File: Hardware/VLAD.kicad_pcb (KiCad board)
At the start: 2 copper layers, 90 x 80 mm, 100 parts, among them J1 BMP388, J2 BNO055, J3 Micro_SD_Card, J4 Conn_01x02_Male, J5 Conn_01x03_Male, J6 Conn_01x02_Male, P1 USB_C_Plug_USB2.0, Q1 S8050, Q2 S8050, Q3 S8550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

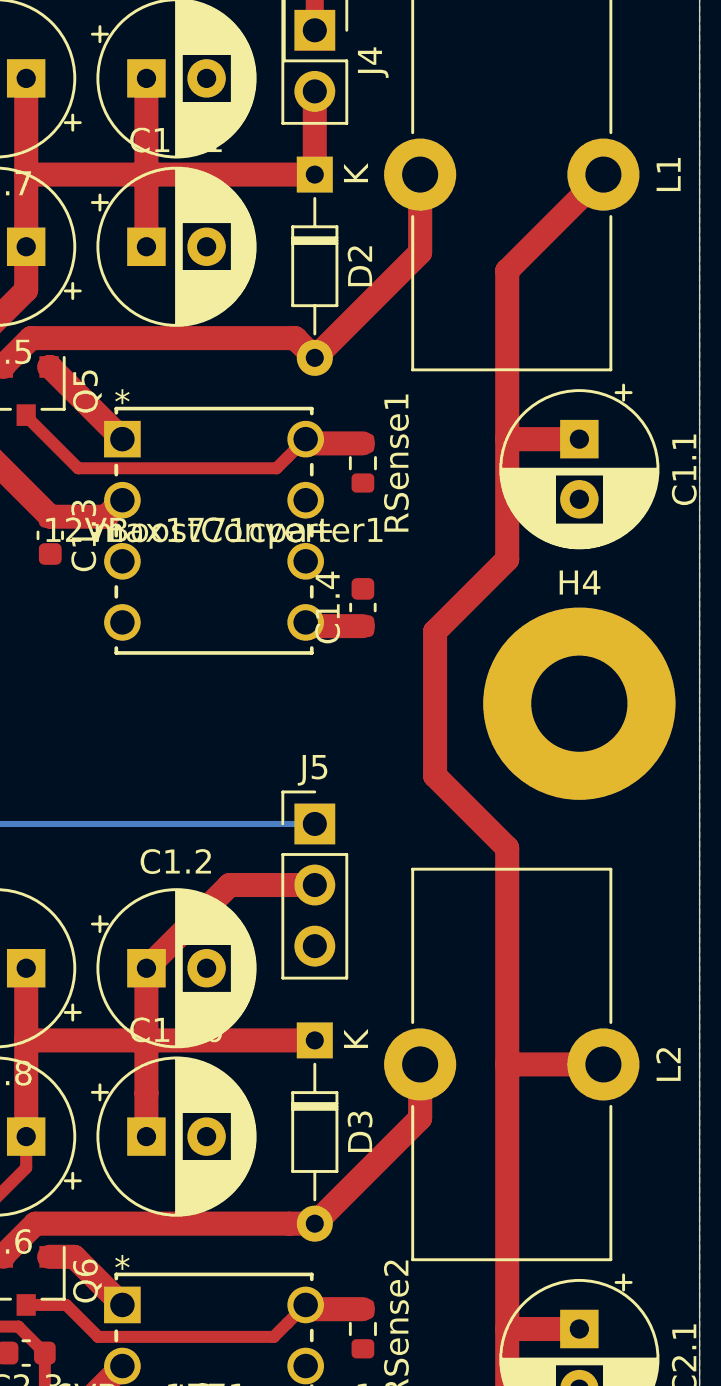
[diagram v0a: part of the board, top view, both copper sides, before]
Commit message: Need some THT - SMD changes
Inductors, capacitors, MAX1771CSA, the LED dudes and the ones next to the ESP
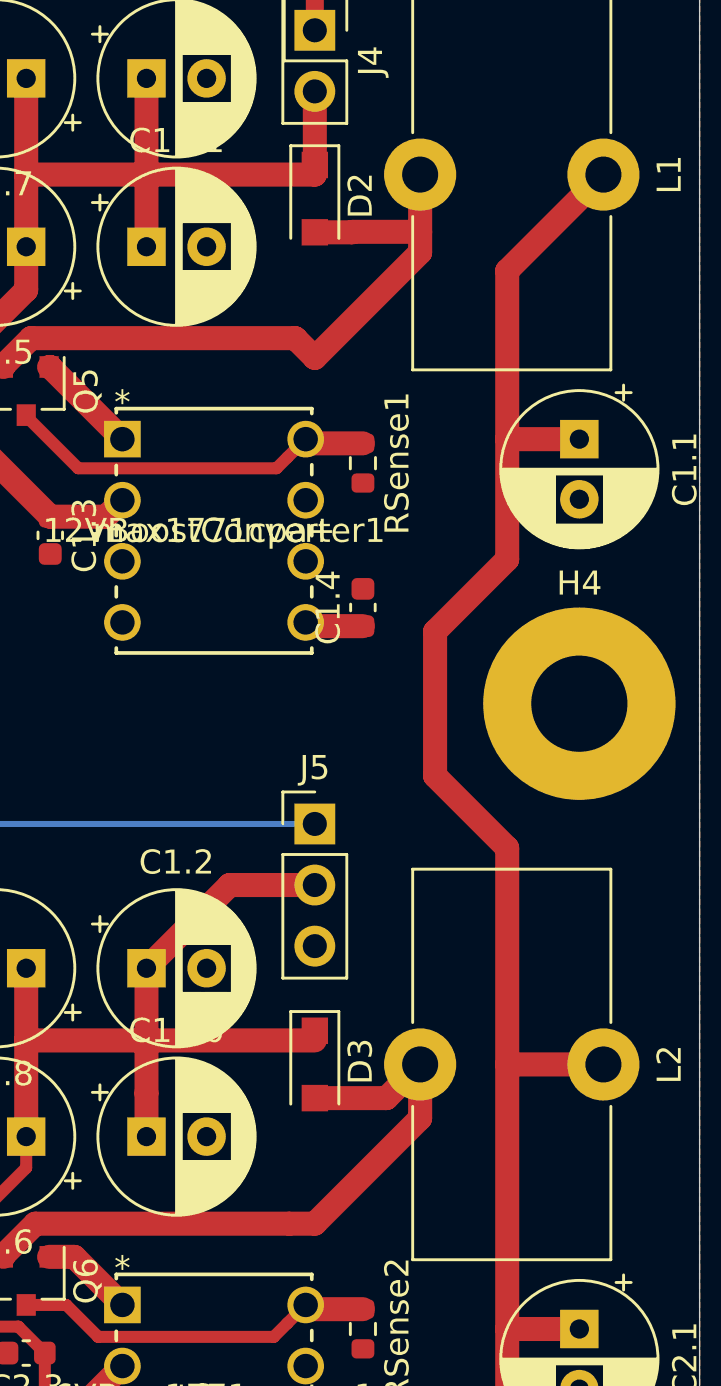
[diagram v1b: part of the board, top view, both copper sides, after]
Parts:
- D2, D3: footprint Diode_THT:D_DO-34_SOD68_P7.62mm_Horizontal -> Diode_SMD:D_SOD-123F
- moved D2 1.00 mm to (94.0, 30.0)
- moved D3 1.00 mm to (94.0, 66.0)
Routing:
- net Net-(D3-Pad2): track 22.0 -> 26.9 mm
- net Net-(D2-Pad2): track 23.3 -> 27.6 mm

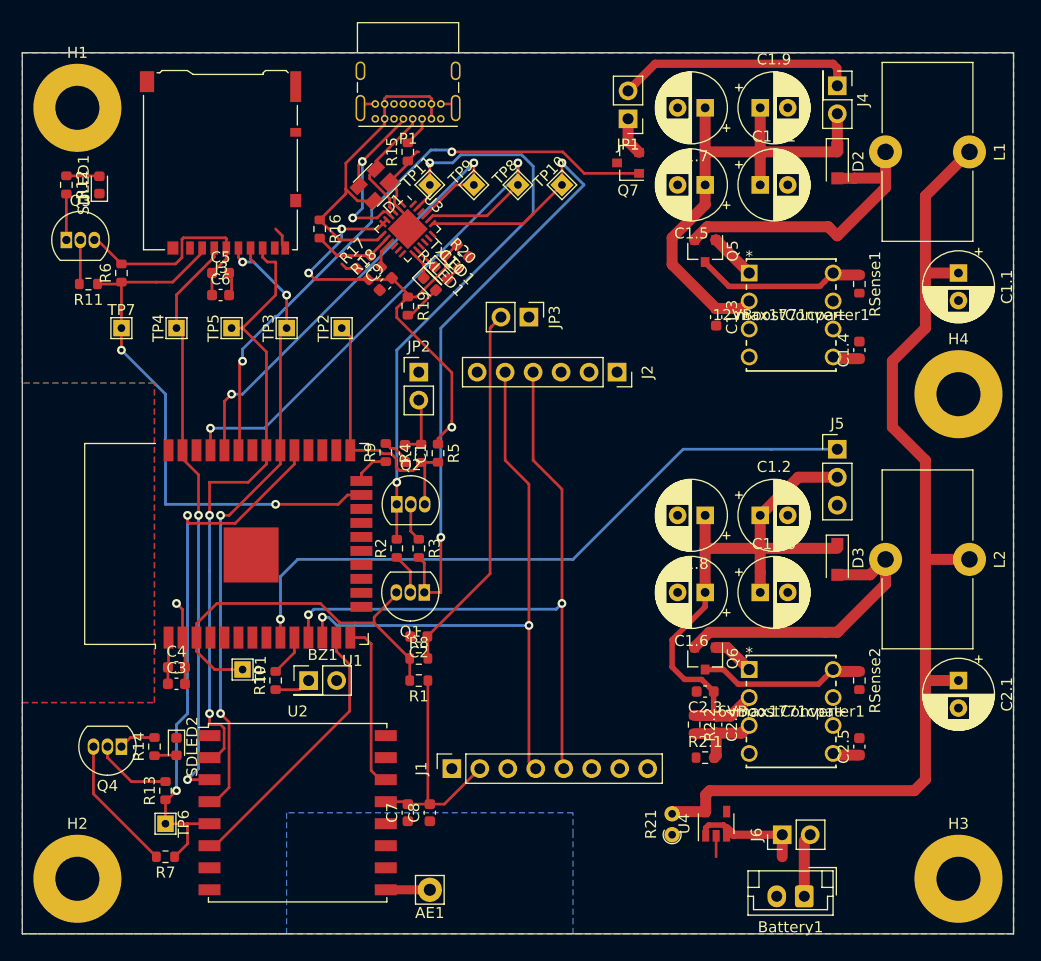
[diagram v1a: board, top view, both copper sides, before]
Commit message: Fixed RF transceiver
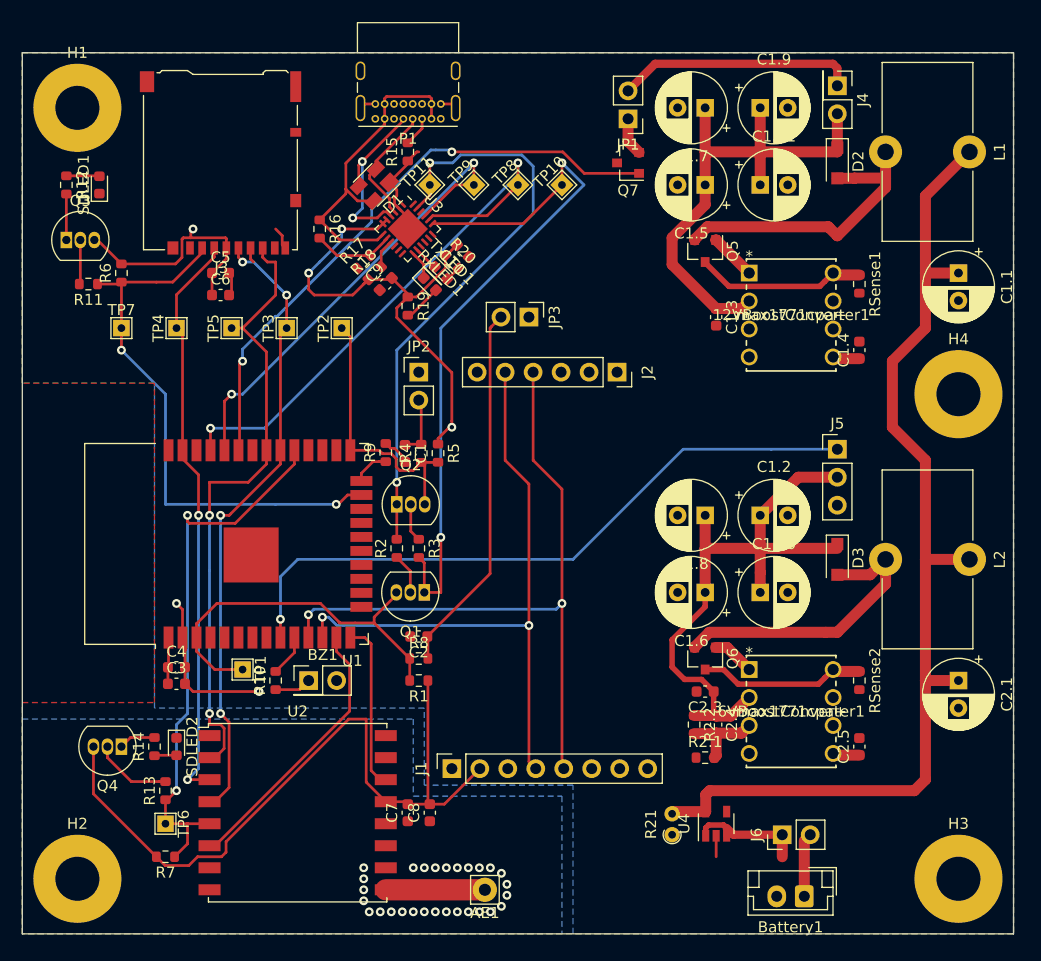
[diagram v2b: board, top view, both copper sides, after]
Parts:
- moved AE1 5.00 mm to (62.0, 96.0)
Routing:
- net +3V3: track 105.8 -> 150.0 mm, vias 4 -> 6
- net Net-(AE1-Pad1): track 4.00 -> 9.00 mm
- net GND: track 28.4 -> 26.8 mm, vias 0 -> 28
- added copper zone on B.Cu, net GND

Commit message: Tried to add footprints. Emphasis on tried.
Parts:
- Q1, Q2: value S8050 -> MMDT2222A; footprint Package_TO_SOT_THT:TO-92_Inline -> Package_TO_SOT_SMD:SOT-363_SC-70-6
- moved Q2 6.08 mm to (60.0, 60.0)
- moved Q1 5.32 mm to (60.0, 65.0), turned to 0 degrees
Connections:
- Q1 pad 1: /USB_RTS -> /EN
- Q1 pad 3: /EN -> (no net)
- Q2 pad 3: /IO0 -> (no net)
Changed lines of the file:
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@@
-(kicad_pcb (version 20171130) (host pcbnew "(5.1.9)-1")
+(kicad_pcb (version 20171130) (host pcbnew "(5.1.4)-1")
   (general
     (thickness 1.6)
@@
   (layers
     (0 F.Cu signal)
-    (31 B.Cu signal)
+    (31 B.Cu signal hide)
     (32 B.Adhes user)
     (33 F.Adhes user)
@@
     (add_net "Net-(U4-Pad4)")
   )
+  (module Package_TO_SOT_SMD:SOT-363_SC-70-6 (layer F.Cu)
+    (at 60 60)
+    (descr "SOT-363, SC-70-6")
+    (tags "SOT-363 SC-70-6")
+    (attr smd)
+    (fp_text reference Q2 (at 0 -2) (layer F.SilkS)
+      (effects (font (size 1 1) (thickness 0.15)))
+    )
+    (fp_text value MMDT2222A (at 0 2 180) (layer F.Fab)
+      (effects (font (size 1 1) (thickness 0.15)))
+    )
+    (fp_line (start -0.175 -1.1) (end -0.675 -0.6) (layer F.Fab) (width 0.1))
+    (fp_line (start 0.675 1.1) (end -0.675 1.1) (layer F.Fab) (width 0.1))
+    (fp_line (start 0.675 -1.1) (end 0.675 1.1) (layer F.Fab) (width 0.1))
+    (fp_line (start -1.6 1.4) (end 1.6 1.4) (layer F.CrtYd) (width 0.05))
+    (fp_line (start -0.675 -0.6) (end -0.675 1.1) (layer F.Fab) (width 0.1))
+    (fp_line (start 0.675 -1.1) (end -0.175 -1.1) (layer F.Fab) (width 0.1))
+    (fp_line (start -1.6 -1.4) (end 1.6 -1.4) (layer F.CrtYd) (width 0.05))
+    (fp_line (start -1.6 -1.4) (end -1.6 1.4) (layer F.CrtYd) (width 0.05))
+    (fp_line (start 1.6 1.4) (end 1.6 -1.4) (layer F.CrtYd) (width 0.05))
+    (fp_line (start -0.7 1.16) (end 0.7 1.16) (layer F.SilkS) (width 0.12))
+    (fp_line (start 0.7 -1.16) (end -1.2 -1.16) (layer F.SilkS) (width 0.12))
+    (fp_text user %R (at 0 0 90) (layer F.Fab)
+      (effects (font (size 0.5 0.5) (thickness 0.075)))
+    )
+    (pad 6 smd rect (at 0.95 -0.65) (size 0.65 0.4) (layers F.Cu F.Paste F.Mask)
+      (net 36 /IO0))
+    (pad 4 smd rect (at 0.95 0.65) (size 0.65 0.4) (layers F.Cu F.Paste F.Mask))
+    (pad 2 smd rect (at -0.95 0) (size 0.65 0.4) (layers F.Cu F.Paste F.Mask)
+      (net 37 "Net-(Q2-Pad2)"))
+    (pad 5 smd rect (at 0.95 0) (size 0.65 0.4) (layers F.Cu F.Paste F.Mask))
+    (pad 3 smd rect (at -0.95 0.65) (size 0.65 0.4) (layers F.Cu F.Paste F.Mask))
+    (pad 1 smd rect (at -0.95 -0.65) (size 0.65 0.4) (layers F.Cu F.Paste F.Mask)
+      (net 35 /USB_DTR))
+    (model ${KISYS3DMOD}/Package_TO_SOT_SMD.3dshapes/SOT-363_SC-70-6.wrl
+      (at (xyz 0 0 0))
+      (scale (xyz 1 1 1))
+      (rotate (xyz 0 0 0))
+    )
+  )
+  (module Package_TO_SOT_SMD:SOT-363_SC-70-6 (layer F.Cu)
+    (at 60 65)
+    (descr "SOT-363, SC-70-6")
+    (tags "SOT-363 SC-70-6")
+    (attr smd)
+    (fp_text reference Q1 (at 0 -2) (layer F.SilkS)
+      (effects (font (size 1 1) (thickness 0.15)))
+    )
+    (fp_text value MMDT2222A (at 0 2 180) (layer F.Fab)
+      (effects (font (size 1 1) (thickness 0.15)))
+    )
+    (fp_line (start -0.175 -1.1) (end -0.675 -0.6) (layer F.Fab) (width 0.1))
+    (fp_line (start 0.675 1.1) (end -0.675 1.1) (layer F.Fab) (width 0.1))
+    (fp_line (start 0.675 -1.1) (end 0.675 1.1) (layer F.Fab) (width 0.1))
+    (fp_line (start -1.6 1.4) (end 1.6 1.4) (layer F.CrtYd) (width 0.05))
+    (fp_line (start -0.675 -0.6) (end -0.675 1.1) (layer F.Fab) (width 0.1))
+    (fp_line (start 0.675 -1.1) (end -0.175 -1.1) (layer F.Fab) (width 0.1))
+    (fp_line (start -1.6 -1.4) (end 1.6 -1.4) (layer F.CrtYd) (width 0.05))
+    (fp_line (start -1.6 -1.4) (end -1.6 1.4) (layer F.CrtYd) (width 0.05))
+    (fp_line (start 1.6 1.4) (end 1.6 -1.4) (layer F.CrtYd) (width 0.05))
+    (fp_line (start -0.7 1.16) (end 0.7 1.16) (layer F.SilkS) (width 0.12))
+    (fp_line (start 0.7 -1.16) (end -1.2 -1.16) (layer F.SilkS) (width 0.12))
+    (fp_text user %R (at 0 0 90) (layer F.Fab)
+      (effects (font (size 0.5 0.5) (thickness 0.075)))
+    )
+    (pad 6 smd rect (at 0.95 -0.65) (size 0.65 0.4) (layers F.Cu F.Paste F.Mask)
+      (net 32 /USB_RTS))
+    (pad 4 smd rect (at 0.95 0.65) (size 0.65 0.4) (layers F.Cu F.Paste F.Mask))
+    (pad 2 smd rect (at -0.95 0) (size 0.65 0.4) (layers F.Cu F.Paste F.Mask)
+      (net 34 "Net-(Q1-Pad2)"))
+    (pad 5 smd rect (at 0.95 0) (size 0.65 0.4) (layers F.Cu F.Paste F.Mask))
+    (pad 3 smd rect (at -0.95 0.65) (size 0.65 0.4) (layers F.Cu F.Paste F.Mask))
+    (pad 1 smd rect (at -0.95 -0.65) (size 0.65 0.4) (layers F.Cu F.Paste F.Mask)
+      (net 33 /EN))
+    (model ${KISYS3DMOD}/Package_TO_SOT_SMD.3dshapes/SOT-363_SC-70-6.wrl
+      (at (xyz 0 0 0))
+      (scale (xyz 1 1 1))
+      (rotate (xyz 0 0 0))
+    )
+  )
   (module Diode_SMD:D_SOD-123F (layer F.Cu)
     (at 94 66 270)
@@
     (model ${KISYS3DMOD}/Package_TO_SOT_THT.3dshapes/TO-92_Inline.wrl
       (at (xyz 0 0 0))
-      (scale (xyz 1 1 1))
-      (rotate (xyz 0 0 0))
-    )
-  )
-  (module Package_TO_SOT_THT:TO-92_Inline (layer F.Cu)
-    (at 54 61)
-    (descr "TO-92 leads in-line, narrow, oval pads, drill 0.75mm (see NXP sot054_po.pdf)")
-    (tags "to-92 sc-43 sc-43a sot54 PA33 transistor")
-    (fp_text reference Q2 (at 1.27 -3.56) (layer F.SilkS)
-      (effects (font (size 1 1) (thickness 0.15)))
-    )
-    (fp_text value S8050 (at 1.27 2.79) (layer F.Fab)
-      (effects (font (size 1 1) (thickness 0.15)))
-    )
-    (fp_line (start 4 2.01) (end -1.46 2.01) (layer F.CrtYd) (width 0.05))
-    (fp_line (start 4 2.01) (end 4 -2.73) (layer F.CrtYd) (width 0.05))
-    (fp_line (start -1.46 -2.73) (end -1.46 2.01) (layer F.CrtYd) (width 0.05))
-    (fp_line (start -1.46 -2.73) (end 4 -2.73) (layer F.CrtYd) (width 0.05))
-    (fp_line (start -0.5 1.75) (end 3 1.75) (layer F.Fab) (width 0.1))
-    (fp_line (start -0.53 1.85) (end 3.07 1.85) (layer F.SilkS) (width 0.12))
-    (fp_arc (start 1.27 0) (end 1.27 -2.6) (angle 135) (layer F.SilkS) (width 0.12))
-    (fp_arc (start 1.27 0) (end 1.27 -2.48) (angle -135) (layer F.Fab) (width 0.1))
-    (fp_arc (start 1.27 0) (end 1.27 -2.6) (angle -135) (layer F.SilkS) (width 0.12))
-    (fp_arc (start 1.27 0) (end 1.27 -2.48) (angle 135) (layer F.Fab) (width 0.1))
-    (fp_text user %R (at 1.27 0) (layer F.Fab)
-      (effects (font (size 1 1) (thickness 0.15)))
-    )
-    (pad 1 thru_hole rect (at 0 0) (size 1.05 1.5) (drill 0.75) (layers *.Cu *.Mask)
-      (net 35 /USB_DTR))
-    (pad 3 thru_hole oval (at 2.54 0) (size 1.05 1.5) (drill 0.75) (layers *.Cu *.Mask)
-      (net 36 /IO0))
-    (pad 2 thru_hole oval (at 1.27 0) (size 1.05 1.5) (drill 0.75) (layers *.Cu *.Mask)
-      (net 37 "Net-(Q2-Pad2)"))
-    (model ${KISYS3DMOD}/Package_TO_SOT_THT.3dshapes/TO-92_Inline.wrl
-      (at (xyz 0 0 0))
-      (scale (xyz 1 1 1))
-      (rotate (xyz 0 0 0))
-    )
-  )
-  (module Package_TO_SOT_THT:TO-92_Inline (layer F.Cu)
-    (at 56.5 69 180)
-    (descr "TO-92 leads in-line, narrow, oval pads, drill 0.75mm (see NXP sot054_po.pdf)")
-    (tags "to-92 sc-43 sc-43a sot54 PA33 transistor")
-    (fp_text reference Q1 (at 1.27 -3.56) (layer F.SilkS)
-      (effects (font (size 1 1) (thickness 0.15)))
-    )
-    (fp_text value S8050 (at 1.27 2.79) (layer F.Fab)
-      (effects (font (size 1 1) (thickness 0.15)))
-    )
-    (fp_line (start 4 2.01) (end -1.46 2.01) (layer F.CrtYd) (width 0.05))
-    (fp_line (start 4 2.01) (end 4 -2.73) (layer F.CrtYd) (width 0.05))
-    (fp_line (start -1.46 -2.73) (end -1.46 2.01) (layer F.CrtYd) (width 0.05))
-    (fp_line (start -1.46 -2.73) (end 4 -2.73) (layer F.CrtYd) (width 0.05))
-    (fp_line (start -0.5 1.75) (end 3 1.75) (layer F.Fab) (width 0.1))
-    (fp_line (start -0.53 1.85) (end 3.07 1.85) (layer F.SilkS) (width 0.12))
-    (fp_arc (start 1.27 0) (end 1.27 -2.6) (angle 135) (layer F.SilkS) (width 0.12))
-    (fp_arc (start 1.27 0) (end 1.27 -2.48) (angle -135) (layer F.Fab) (width 0.1))
-    (fp_arc (start 1.27 0) (end 1.27 -2.6) (angle -135) (layer F.SilkS) (width 0.12))
-    (fp_arc (start 1.27 0) (end 1.27 -2.48) (angle 135) (layer F.Fab) (width 0.1))
-    (fp_text user %R (at 1.27 0) (layer F.Fab)
-      (effects (font (size 1 1) (thickness 0.15)))
-    )
-    (pad 1 thru_hole rect (at 0 0 180) (size 1.05 1.5) (drill 0.75) (layers *.Cu *.Mask)
-      (net 32 /USB_RTS))
-    (pad 3 thru_hole oval (at 2.54 0 180) (size 1.05 1.5) (drill 0.75) (layers *.Cu *.Mask)
-      (net 33 /EN))
-    (pad 2 thru_hole oval (at 1.27 0 180) (size 1.05 1.5) (drill 0.75) (layers *.Cu *.Mask)
-      (net 34 "Net-(Q1-Pad2)"))
-    (model ${KISYS3DMOD}/Package_TO_SOT_THT.3dshapes/TO-92_Inline.wrl
-      (at (xyz 0 0 0))
